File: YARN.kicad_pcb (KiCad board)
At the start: 2 copper layers, 99 x 91.7 mm, 35 parts, among them J1 Cart System Out, J2 Cart Sub In, J3 Cart Main In, U1 EXP Addressing Decoder ROM

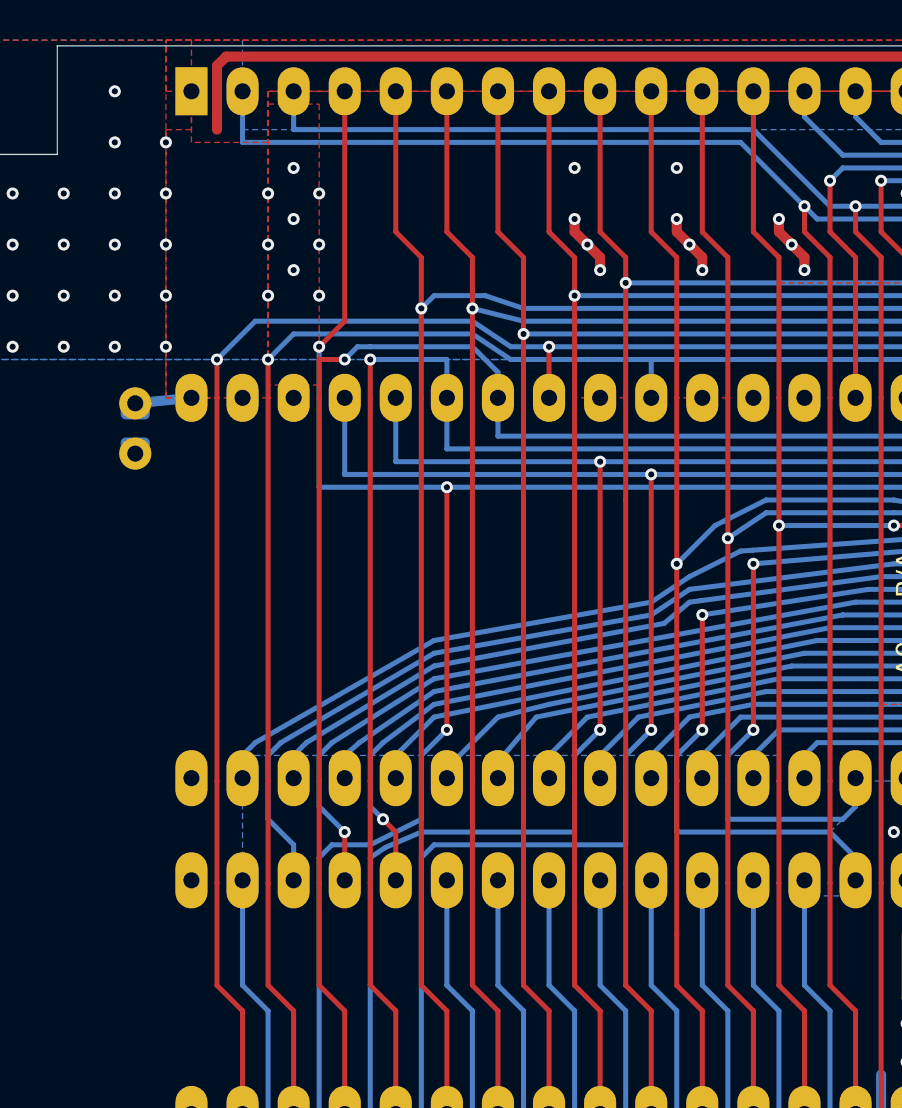
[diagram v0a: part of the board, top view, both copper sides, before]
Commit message: Fix copper fills
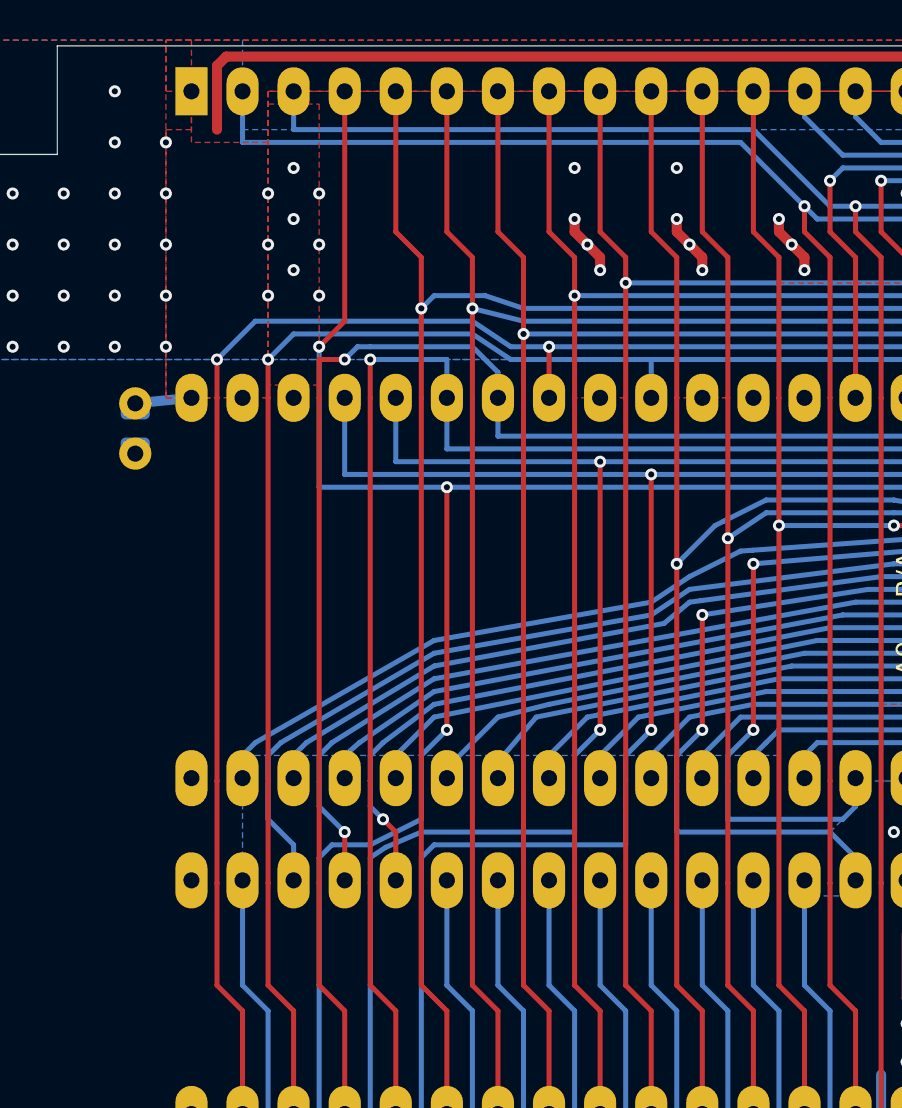
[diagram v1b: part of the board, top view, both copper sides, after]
